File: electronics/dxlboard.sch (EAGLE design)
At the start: 49 parts

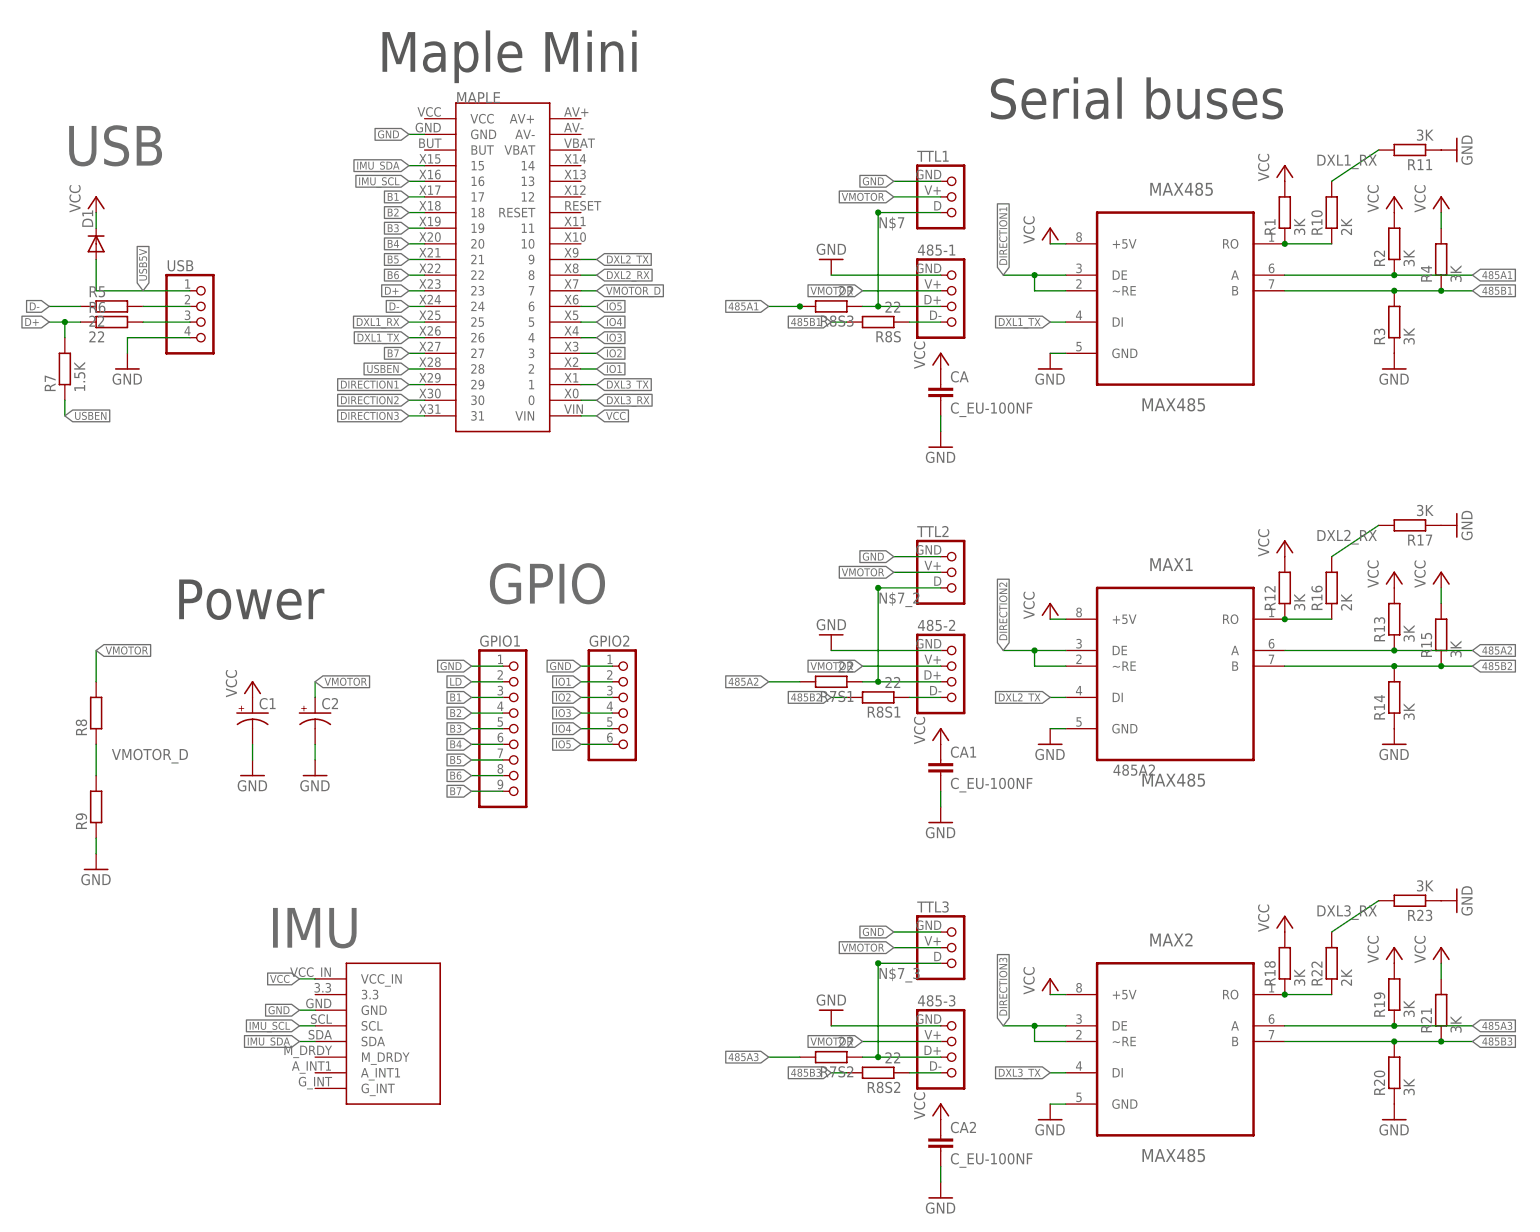
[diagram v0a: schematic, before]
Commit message: Updating FARNELL attributes & making BOM
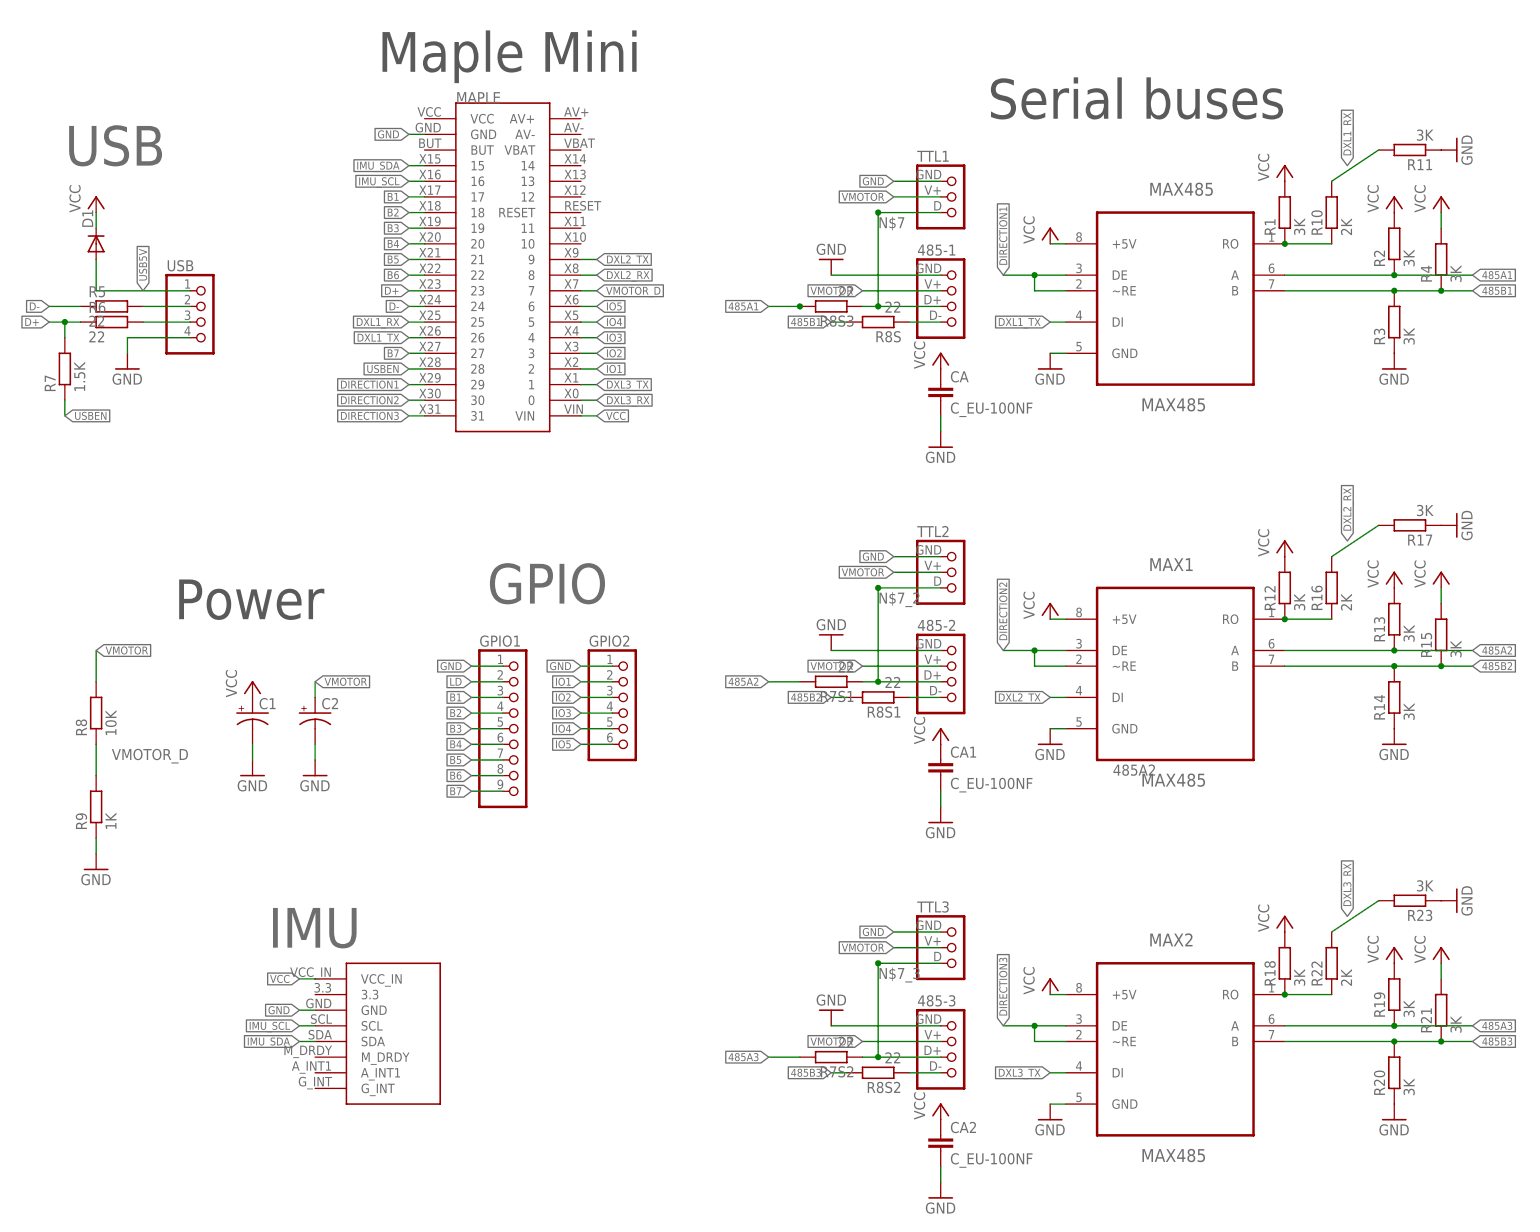
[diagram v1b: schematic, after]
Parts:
- C1, C2: FARNELL (none) -> 1144619
- CA, CA1, CA2: FARNELL (none) -> 2688486RL
- GPIO1, GPIO2, USB: FARNELL (none) -> -
- R1, R11, R12, R13, R14, R15, R17, R18, R19, R2, R20, R21, R23, R3, R4: FARNELL (none) -> 2074431
- R10, R16, R22: FARNELL (none) -> 2447622
- R5, R6, R7S1, R7S2, R8S, R8S1, R8S2, R8S3: FARNELL (none) -> 2446926
- R7: FARNELL (none) -> 2447592
- R8: value (none) -> 10K; FARNELL (none) -> 2074334RL
- R9: value (none) -> 1K; FARNELL (none) -> 2074332RL
